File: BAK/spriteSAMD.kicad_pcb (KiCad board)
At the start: 4 copper layers, 35 x 35 mm, 39 parts, among them IC1 BMX160, J1 Conn_01x01, J2 10118194-0001LF, J28 Conn_01x01, J29 Conn_01x01, J3 Micro_SD_Card, J30 Conn_01x01, J4 xf2m-2415-1a, J5 XF2M-1015-1A, J6 Conn_01x02, SW1 KMR231NG LFS, U1 RFM95W-915S2, U2 ATSAMD51G_TQFN48, U3 DRV8833PWP, U4 TPS82740BSIPR, U5 DRV8833PWP, U6 MAX708RESA-T, U8 RFM95W-915S2, X1 ANTENNA_U.FL, X2 ANTENNA_U.FL

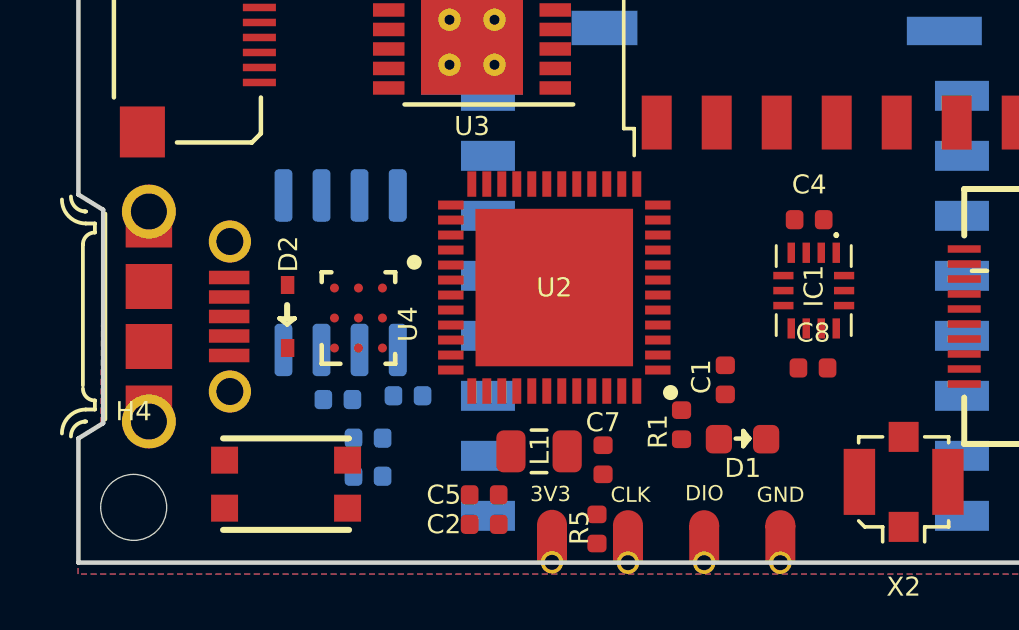
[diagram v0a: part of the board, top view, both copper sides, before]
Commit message: Moved RBF Header to under micro USB port
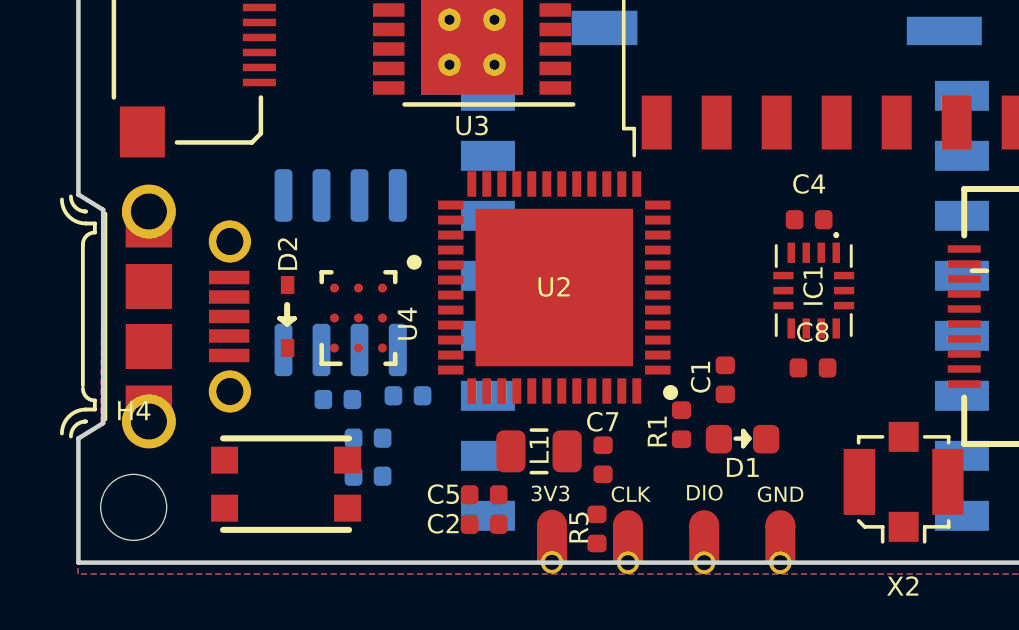
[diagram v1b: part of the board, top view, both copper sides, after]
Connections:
- net ~RESET renamed ~{RESET}
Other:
- net class Default removed
